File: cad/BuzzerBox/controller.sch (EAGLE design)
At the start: 122 parts, among them Q1 BSS138, Q2 BSS138, T1 BC849, T10 BC849, T2 BC849, T3 BC849, T4 BC849, T5 BC849, T6 BC849, T7 BC849, T8 BC849, T9 BC849

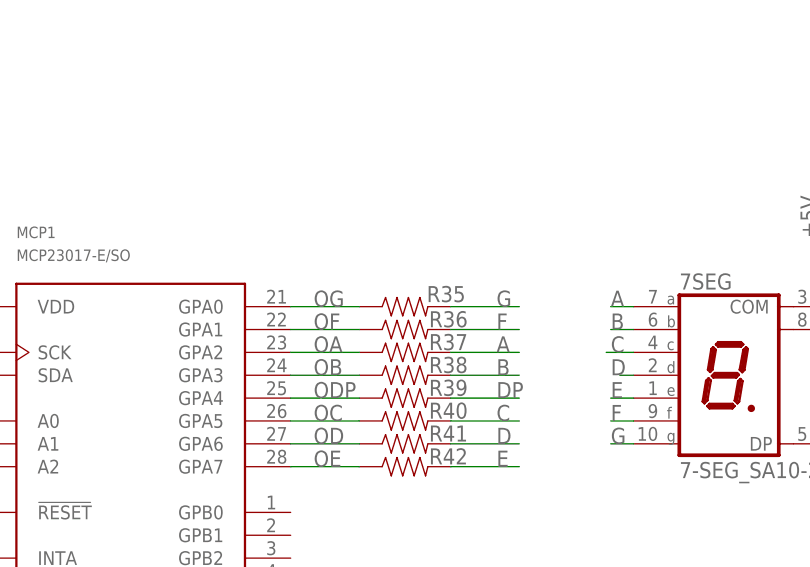
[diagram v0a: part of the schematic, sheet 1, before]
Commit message: Update resistor values for BOM
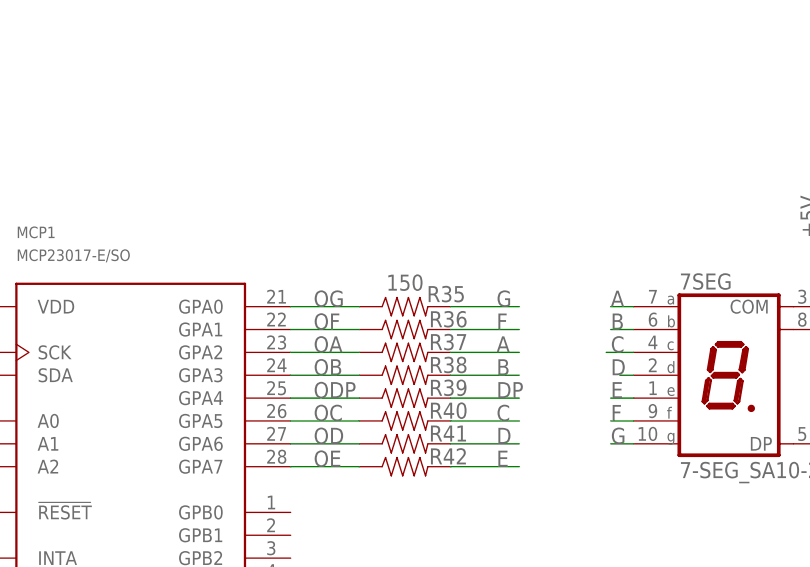
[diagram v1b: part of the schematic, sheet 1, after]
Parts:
- R35, R36, R37, R38, R39, R40, R41, R42: value (none) -> 150
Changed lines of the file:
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@@
 <part name="7SEG" library="display-kingbright" library_urn="urn:adsk.eagle:library:213" deviceset="7-SEG_" device="SA10-21" package3d_urn="urn:adsk.eagle:package:13078/1"/>
 <part name="P+2" library="supply1" library_urn="urn:adsk.eagle:library:371" deviceset="+5V" device=""/>
-<part name="R35" library="SparkFun-Resistors" library_urn="urn:adsk.eagle:library:532" deviceset="RESISTOR" device="0805" package3d_urn="urn:adsk.eagle:package:39651/1" value=" "/>
-<part name="R36" library="SparkFun-Resistors" library_urn="urn:adsk.eagle:library:532" deviceset="RESISTOR" device="0805" package3d_urn="urn:adsk.eagle:package:39651/1" value=" "/>
-<part name="R37" library="SparkFun-Resistors" library_urn="urn:adsk.eagle:library:532" deviceset="RESISTOR" device="0805" package3d_urn="urn:adsk.eagle:package:39651/1" value=" "/>
-<part name="R38" library="SparkFun-Resistors" library_urn="urn:adsk.eagle:library:532" deviceset="RESISTOR" device="0805" package3d_urn="urn:adsk.eagle:package:39651/1" value=" "/>
-<part name="R39" library="SparkFun-Resistors" library_urn="urn:adsk.eagle:library:532" deviceset="RESISTOR" device="0805" package3d_urn="urn:adsk.eagle:package:39651/1" value=" "/>
-<part name="R40" library="SparkFun-Resistors" library_urn="urn:adsk.eagle:library:532" deviceset="RESISTOR" device="0805" package3d_urn="urn:adsk.eagle:package:39651/1" value=" "/>
-<part name="R41" library="SparkFun-Resistors" library_urn="urn:adsk.eagle:library:532" deviceset="RESISTOR" device="0805" package3d_urn="urn:adsk.eagle:package:39651/1" value=" "/>
-<part name="R42" library="SparkFun-Resistors" library_urn="urn:adsk.eagle:library:532" deviceset="RESISTOR" device="0805" package3d_urn="urn:adsk.eagle:package:39651/1" value=" "/>
+<part name="R35" library="SparkFun-Resistors" library_urn="urn:adsk.eagle:library:532" deviceset="RESISTOR" device="0805" package3d_urn="urn:adsk.eagle:package:39651/1" value="150"/>
+<part name="R36" library="SparkFun-Resistors" library_urn="urn:adsk.eagle:library:532" deviceset="RESISTOR" device="0805" package3d_urn="urn:adsk.eagle:package:39651/1" value="150"/>
+<part name="R37" library="SparkFun-Resistors" library_urn="urn:adsk.eagle:library:532" deviceset="RESISTOR" device="0805" package3d_urn="urn:adsk.eagle:package:39651/1" value="150"/>
+<part name="R38" library="SparkFun-Resistors" library_urn="urn:adsk.eagle:library:532" deviceset="RESISTOR" device="0805" package3d_urn="urn:adsk.eagle:package:39651/1" value="150"/>
+<part name="R39" library="SparkFun-Resistors" library_urn="urn:adsk.eagle:library:532" deviceset="RESISTOR" device="0805" package3d_urn="urn:adsk.eagle:package:39651/1" value="150"/>
+<part name="R40" library="SparkFun-Resistors" library_urn="urn:adsk.eagle:library:532" deviceset="RESISTOR" device="0805" package3d_urn="urn:adsk.eagle:package:39651/1" value="150"/>
+<part name="R41" library="SparkFun-Resistors" library_urn="urn:adsk.eagle:library:532" deviceset="RESISTOR" device="0805" package3d_urn="urn:adsk.eagle:package:39651/1" value="150"/>
+<part name="R42" library="SparkFun-Resistors" library_urn="urn:adsk.eagle:library:532" deviceset="RESISTOR" device="0805" package3d_urn="urn:adsk.eagle:package:39651/1" value="150"/>
 <part name="MCP1" library="microchip" deviceset="MCP23017" device="-E/SO"/>
 <part name="GND24" library="supply1" library_urn="urn:adsk.eagle:library:371" deviceset="GND" device=""/>
@@
 <instance part="R35" gate="G$1" x="81.28" y="91.44" smashed="yes">
 <attribute name="NAME" x="85.852" y="91.948" size="1.778" layer="95" font="vector" align="bottom-center"/>
-<attribute name="VALUE" x="81.28" y="89.916" size="1.778" layer="96" font="vector" align="top-center"/>
+<attribute name="VALUE" x="81.28" y="94.996" size="1.778" layer="96" font="vector" align="top-center"/>
 </instance>
 <instance part="R36" gate="G$1" x="81.28" y="88.9" smashed="yes">
 <attribute name="NAME" x="86.106" y="89.154" size="1.778" layer="95" font="vector" align="bottom-center"/>
-<attribute name="VALUE" x="81.28" y="87.376" size="1.778" layer="96" font="vector" align="top-center"/>
 </instance>
 <instance part="R37" gate="G$1" x="81.28" y="86.36" smashed="yes">
 <attribute name="NAME" x="86.106" y="86.614" size="1.778" layer="95" font="vector" align="bottom-center"/>
-<attribute name="VALUE" x="81.28" y="84.836" size="1.778" layer="96" font="vector" align="top-center"/>
 </instance>
 <instance part="R38" gate="G$1" x="81.28" y="83.82" smashed="yes">
 <attribute name="NAME" x="86.106" y="84.074" size="1.778" layer="95" font="vector" align="bottom-center"/>
-<attribute name="VALUE" x="81.28" y="82.296" size="1.778" layer="96" font="vector" align="top-center"/>
 </instance>
 <instance part="R39" gate="G$1" x="81.28" y="81.28" smashed="yes">
 <attribute name="NAME" x="86.106" y="81.534" size="1.778" layer="95" font="vector" align="bottom-center"/>
-<attribute name="VALUE" x="81.28" y="79.756" size="1.778" layer="96" font="vector" align="top-center"/>
 </instance>
 <instance part="R40" gate="G$1" x="81.28" y="78.74" smashed="yes">
 <attribute name="NAME" x="86.106" y="78.994" size="1.778" layer="95" font="vector" align="bottom-center"/>
-<attribute name="VALUE" x="81.28" y="77.216" size="1.778" layer="96" font="vector" align="top-center"/>
 </instance>
 <instance part="R41" gate="G$1" x="81.28" y="76.2" smashed="yes">
 <attribute name="NAME" x="86.106" y="76.454" size="1.778" layer="95" font="vector" align="bottom-center"/>
-<attribute name="VALUE" x="81.28" y="74.676" size="1.778" layer="96" font="vector" align="top-center"/>
 </instance>
 <instance part="R42" gate="G$1" x="81.28" y="73.66" smashed="yes">
 <attribute name="NAME" x="86.106" y="73.914" size="1.778" layer="95" font="vector" align="bottom-center"/>
-<attribute name="VALUE" x="78.74" y="72.136" size="1.778" layer="96" font="vector" align="top-center"/>
 </instance>
 <instance part="MCP1" gate="G$1" x="50.8" y="71.12" smashed="yes">

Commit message: Upgrade LED output resistors to bigger 2512 package to better handle larger currents
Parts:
- R46, R48, R50, R52, R54, R56, R58, R60, R62, R64: device SparkFun-Resistors:RESISTOR0805 -> rcl:R-EU_R2512

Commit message: Replaced Arduino with bare uC
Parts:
- removed D1, D2: 1N4002, diode:1N4004
- removed JP1: (no value), jumper:JP2E
- removed LDO1: LM1084-V, v-reg-2:LM1084-V
- removed PRO_MICRO: SPARKFUN_PRO_MICRO, SparkFun-Boards:SPARKFUN_PRO_MICRO
- removed R65: 330, SparkFun-Resistors:RESISTOR0805
- removed R66: 220, SparkFun-Resistors:RESISTOR0805
- added C3: 1uF, Condensatori:0006_1UF_0603/GRM188R61E105KA12D
- added C5: 4,7uF_16V, Condensatori:0833_TAJA475MO16RNJ
- added J4: (no value), Connettori:0114_PH254-203DF118A00V
- added RPI-CM1: RPI-CM4, RPI-CM4:RPI-CM4
- added U1: ATMEGA328P-AU, Atmel-ATMEGA328P-AU:ATMEGA328P-AU
- added Y1: 16MHz, Cristalli:0011_CSTCE16M0V53-R0
- C1: value 0.1uF -> 100nF; device rcl:C-EU075-052X106 -> Condensatori:0015_100NF_0603
- C2: device resistor:CPOL-US085CS-1AR -> Condensatori:0006_1UF_0603/GRM188R61E105KA12D
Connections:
- removed net +12V: C1.1, D1.C, JP1.3, LDO1.IN
- removed net D11: C16.1, PRO_MICRO.11(MOSI), R29.2, R30.1
- removed net D13: C8.1, PRO_MICRO.13(SCK), R5.2, R6.1
- new net A1: U1.PC1
- new net A2: U1.PC2
- new net A3: C13.1, R20.2, R21.1, U1.PC3
- new net D2: U1.PD2
- new net D3: C14.1, R23.2, R24.1, U1.PD3
- new net MISO: J4.1, U1.PB4
- new net MOSI: J4.4, U1.PB3
- new net N$44: C1.1, U1.AREF
- new net N$48: U1.PD1
- new net N$49: U1.PD0
- new net RESET: J4.5, U1.PC6
- new net SCK: J4.3, U1.PB5
- net +5V: now also C2.1, C3.1, C5.+, D3.C, J4.2, RPI-CM1G$1.+5V(INPUT)@77, RPI-CM1G$1.+5V(INPUT)@79, RPI-CM1G$1.+5V(INPUT)@81, RPI-CM1G$1.+5V(INPUT)@83, RPI-CM1G$1.+5V(INPUT)@85, RPI-CM1G$1.+5V(INPUT)@87, U1.AVCC, U1.VCC, U1.VCC_2; no longer C2.+, D1.A, D2.C, JP1.1, LDO1.OUT, PRO_MICRO.VCC, R66.2
- net A0: now also U1.PC0; no longer PRO_MICRO.A0
- net D10: now also C16.1, R29.2, R30.1, U1.PB2; no longer C15.1, PRO_MICRO.*10, R26.2, R27.1
- net D12: no longer PRO_MICRO.12(MISO)
- net D4: now also C12.1, R17.2, R18.1, U1.PD4; no longer C9.1, PRO_MICRO.4, R8.2, R9.1
- net D5: now also C11.1, R15.2, R16.1, U1.PD5; no longer C10.1, PRO_MICRO.*5, R12.2, R13.1
- net D6: now also C10.1, R12.2, R13.1, U1.PD6; no longer C11.1, PRO_MICRO.*6, R15.2, R16.1
- net D7: now also C9.1, R8.2, R9.1, U1.PD7; no longer C12.1, PRO_MICRO.7, R17.2, R18.1
- net D8: now also C8.1, R5.2, R6.1, U1.PB0; no longer C13.1, PRO_MICRO.8, R20.2, R21.1
- net D9: now also C15.1, R26.2, R27.1, U1.PB1; no longer C14.1, PRO_MICRO.*9, R23.2, R24.1
- net GND: now also C2.2, C3.2, C5.-, J4.6, RPI-CM1G$1.GND@1, RPI-CM1G$1.GND@13, RPI-CM1G$1.GND@14, RPI-CM1G$1.GND@2, RPI-CM1G$1.GND@22, RPI-CM1G$1.GND@23, RPI-CM1G$1.GND@32, RPI-CM1G$1.GND@33, RPI-CM1G$1.GND@42, RPI-CM1G$1.GND@43, RPI-CM1G$1.GND@52, RPI-CM1G$1.GND@53, RPI-CM1G$1.GND@59, RPI-CM1G$1.GND@60, RPI-CM1G$1.GND@65, RPI-CM1G$1.GND@66, RPI-CM1G$1.GND@7, RPI-CM1G$1.GND@71, RPI-CM1G$1.GND@74, RPI-CM1G$1.GND@8, RPI-CM1G$1.GND@98, U1.GND, U1.GND_2, U1.GND_3, Y1.2; no longer C2.-, D2.A, PRO_MICRO.GND, PRO_MICRO.GND@1, R65.1
- net N$33: now also U1.PB7, Y1.3; no longer D3.C, JP1.2
- net N$43: now also U1.PB6, Y1.1; no longer LDO1.ADJ, R65.2, R66.1
- net SCL: now also U1.PC5; no longer PRO_MICRO.*3
- net SDA: now also U1.PC4; no longer PRO_MICRO.2
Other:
- note added: "ICSP"
- note removed: "5V Voltage Regulator"
- note removed: "5V, 500mA"
- note removed: "C2 of 1 µF tantalum capacitor on the output helps to improve transient response"
- note removed: "D1 protect the device against input short circuit"
- note removed: "D2 protect against output short circuit for capacitance discharging"
- note removed: "Useful Notes"
- moved on the sheet: C1

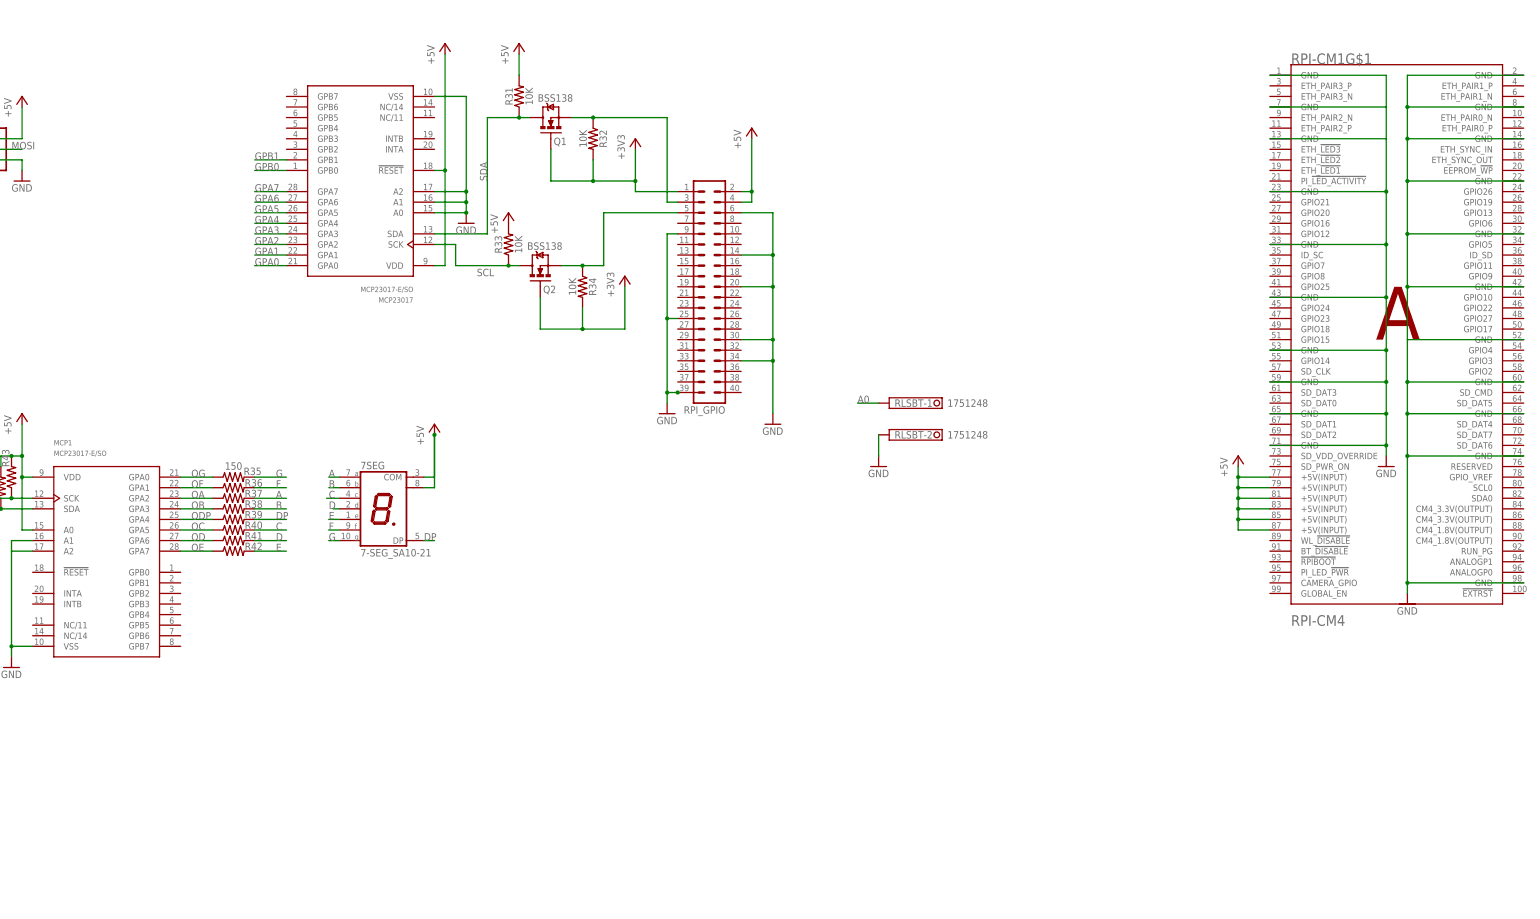
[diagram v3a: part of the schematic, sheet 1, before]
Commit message: Start adding the RPi CM4
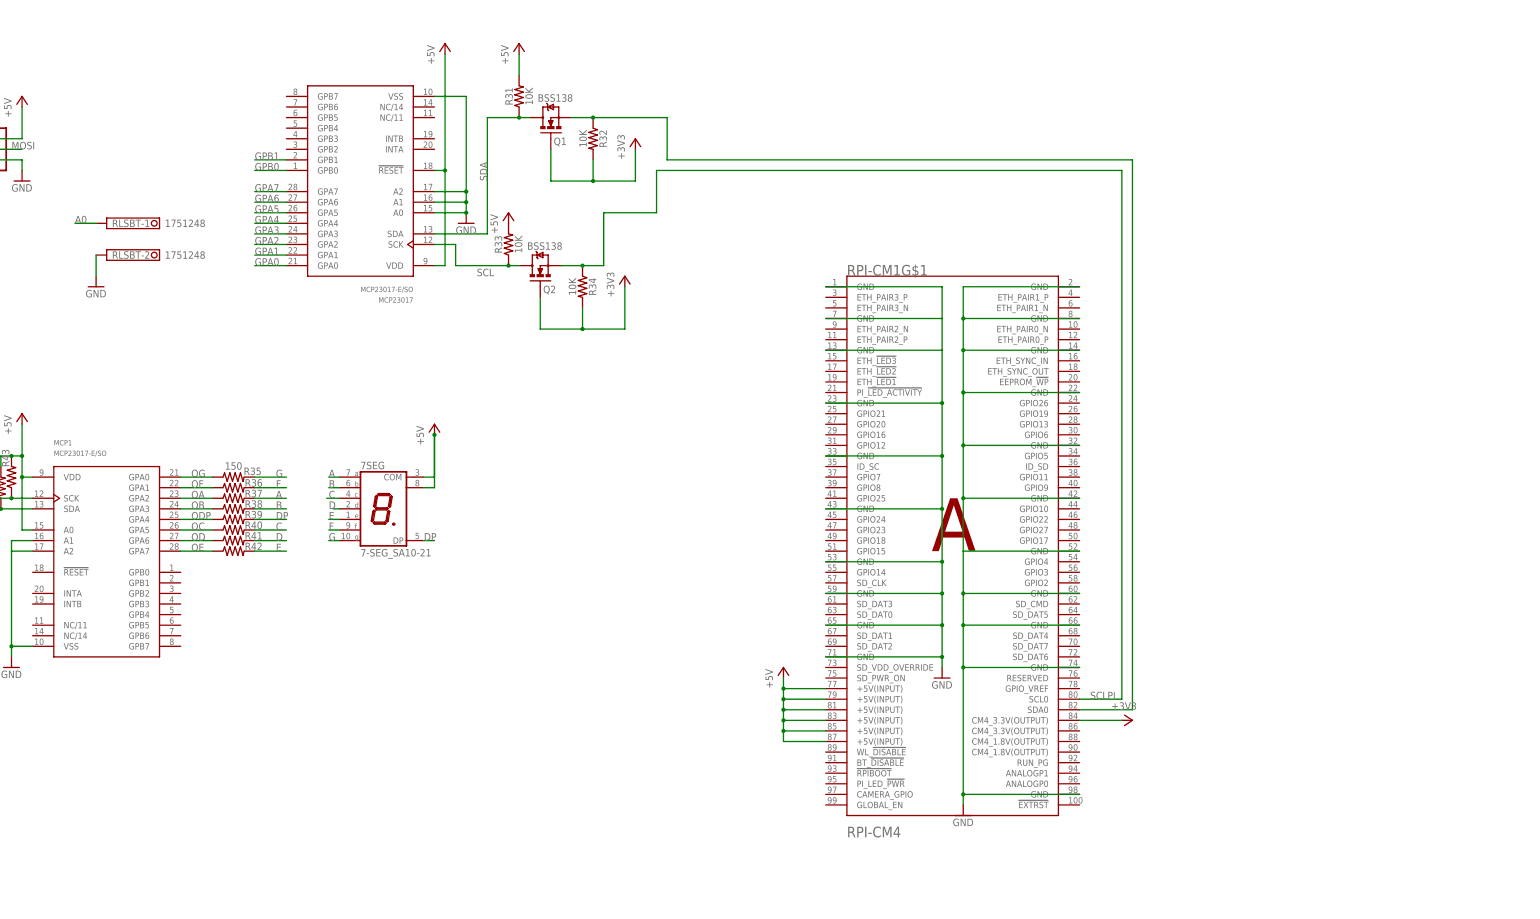
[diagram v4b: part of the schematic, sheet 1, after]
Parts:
- removed RPI_GPIO: (no value), con-lstb:MA20-2
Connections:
- removed net N$42: Q2.S, R34.1, RPI_GPIO.5
- new net SCLPI: Q2.S, R34.1, RPI-CM1G$1.SCL0
- net +3V3: now also RPI-CM1G$1.CM4_3.3V(OUTPUT)@84; no longer RPI_GPIO.1
- net +5V: no longer RPI_GPIO.2, RPI_GPIO.4
- net GND: no longer RPI_GPIO.14, RPI_GPIO.20, RPI_GPIO.25, RPI_GPIO.30, RPI_GPIO.34, RPI_GPIO.39, RPI_GPIO.6, RPI_GPIO.9
- net N$41: now also RPI-CM1G$1.SDA0; no longer RPI_GPIO.3
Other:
- moved on the sheet: RLSBT-1, RLSBT-2, RPI-CM1G$1
